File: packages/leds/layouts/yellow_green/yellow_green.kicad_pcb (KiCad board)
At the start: 2 copper layers, 2 parts, among them U1 2.1V

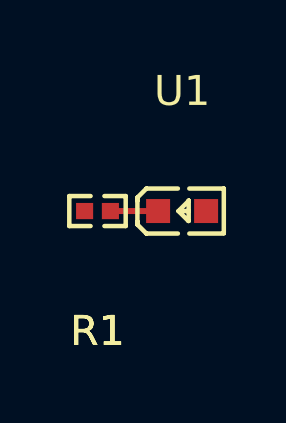
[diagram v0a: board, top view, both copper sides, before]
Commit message: rebuild all packages & regenerate images of changed layouts (silk)
Add new scripts for version bump and build (based on atopile/packages)
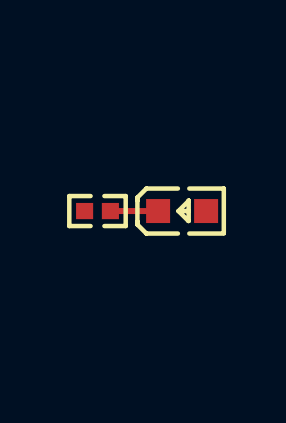
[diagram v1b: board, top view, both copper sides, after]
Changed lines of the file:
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@@
             (at 0 -4 0)
             (layer "F.SilkS")
-            (hide no)
+            (hide yes)
             (effects
                 (font
@@
                     (thickness 0.15)
                 )
+                (hide yes)
             )
             (unlocked no)
@@
                     (thickness 0.15)
                 )
+                (hide yes)
             )
             (unlocked no)
@@
             (at 0 -4 0)
             (layer "F.SilkS")
-            (hide no)
+            (hide yes)
             (effects
                 (font
@@
             )
         )
-        (property "checksum" "ce7edd47c3b4647bff313dd93c39255c9bdec85535db3753d3b458911968ac2b"
+        (property "checksum" "779ca8754790a5438c2a09389b067251dbfa7222c0248148db0ea64f1317a83a"
             (at 0 0 0)
             (layer "User.9")
@@
             )
         )
-        (property "__atopile_lib_fp_hash__" "4ba5d011-6340-9355-9d36-4b761e8a1e52"
+        (property "__atopile_lib_fp_hash__" "e46c8e29-9811-abad-c164-49162da2fbc2"
             (at 0 0 0)
             (layer "User.9")
@@
                     (thickness 0.15)
                 )
+                (hide yes)
             )
             (unlocked no)
